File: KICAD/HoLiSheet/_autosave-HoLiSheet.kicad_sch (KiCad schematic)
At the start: 8 parts, among them J1 Conn_01x06, J3 Conn_01x06

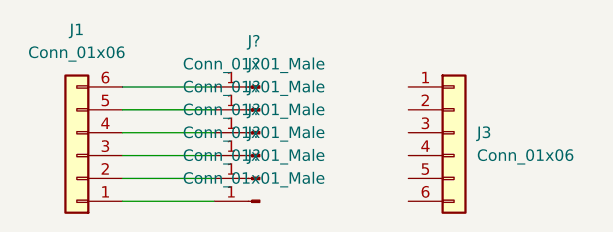
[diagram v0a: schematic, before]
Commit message: Adding new standalone CAD and new iamges
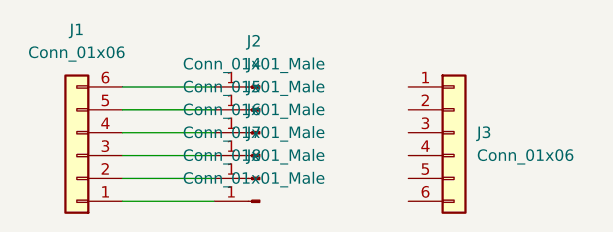
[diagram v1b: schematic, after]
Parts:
- removed J? (x5): Conn_01x01_Male, symbol Connector:Conn_01x01_Male
- added J4, J5, J6, J7, J8: Conn_01x01_Male, footprints:PinHeader_1x01_P1.00mm_Horizontal, symbol Connector:Conn_01x01_Male
- J2: renamed from J?; footprint (none) -> footprints:PinHeader_1x01_P1.00mm_Horizontal
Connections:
- net at J1.1 (Pin_1): now also J8.1 (Pin_1)
- net at J1.2 (Pin_2): now also J7.1 (Pin_1)
- net at J1.3 (Pin_3): now also J6.1 (Pin_1)
- net at J1.4 (Pin_4): now also J5.1 (Pin_1)
- net at J1.5 (Pin_5): now also J4.1 (Pin_1)
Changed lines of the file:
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@@
     (pin "6")
   )
-  (symbol (lib_id "Connector:Conn_01x01_Male") (at 118.11 71.12 180) (unit 1)
+  (symbol (lib_id "Connector:Conn_01x01_Male") (at 118.11 76.2 180) (unit 1)
     (in_bom yes) (on_board yes) (fields_autoplaced)
-    (property "Reference" "J?" (id 0) (at 117.475 66.04 0))
-    (property "Value" "Conn_01x01_Male" (id 1) (at 117.475 68.58 0))
-    (property "Footprint" "" (id 2) (at 118.11 71.12 0)
+    (property "Reference" "J8" (id 0) (at 117.475 71.12 0))
+    (property "Value" "Conn_01x01_Male" (id 1) (at 117.475 73.66 0))
+    (property "Footprint" "footprints:PinHeader_1x01_P1.00mm_Horizontal" (id 2) (at 118.11 76.2 0)
       (effects (font (size 1.27 1.27)) hide)
     )
-    (property "Datasheet" "~" (id 3) (at 118.11 71.12 0)
+    (property "Datasheet" "~" (id 3) (at 118.11 76.2 0)
+      (effects (font (size 1.27 1.27)) hide)
+    )
+    (pin "1")
+  )
+  (symbol (lib_id "Connector:Conn_01x01_Male") (at 118.11 66.04 180) (unit 1)
+    (in_bom yes) (on_board yes) (fields_autoplaced)
+    (property "Reference" "J4" (id 0) (at 117.475 60.96 0))
+    (property "Value" "Conn_01x01_Male" (id 1) (at 117.475 63.5 0))
+    (property "Footprint" "footprints:PinHeader_1x01_P1.00mm_Horizontal" (id 2) (at 118.11 66.04 0)
+      (effects (font (size 1.27 1.27)) hide)
+    )
+    (property "Datasheet" "~" (id 3) (at 118.11 66.04 0)
       (effects (font (size 1.27 1.27)) hide)
     )
@@
   (symbol (lib_id "Connector:Conn_01x01_Male") (at 118.11 68.58 180) (unit 1)
     (in_bom yes) (on_board yes) (fields_autoplaced)
-    (property "Reference" "J?" (id 0) (at 117.475 63.5 0))
+    (property "Reference" "J5" (id 0) (at 117.475 63.5 0))
     (property "Value" "Conn_01x01_Male" (id 1) (at 117.475 66.04 0))
-    (property "Footprint" "" (id 2) (at 118.11 68.58 0)
+    (property "Footprint" "footprints:PinHeader_1x01_P1.00mm_Horizontal" (id 2) (at 118.11 68.58 0)
       (effects (font (size 1.27 1.27)) hide)
     )
     (property "Datasheet" "~" (id 3) (at 118.11 68.58 0)
+      (effects (font (size 1.27 1.27)) hide)
+    )
+    (pin "1")
+  )
+  (symbol (lib_id "Connector:Conn_01x01_Male") (at 118.11 71.12 180) (unit 1)
+    (in_bom yes) (on_board yes) (fields_autoplaced)
+    (property "Reference" "J6" (id 0) (at 117.475 66.04 0))
+    (property "Value" "Conn_01x01_Male" (id 1) (at 117.475 68.58 0))
+    (property "Footprint" "footprints:PinHeader_1x01_P1.00mm_Horizontal" (id 2) (at 118.11 71.12 0)
+      (effects (font (size 1.27 1.27)) hide)
+    )
+    (property "Datasheet" "~" (id 3) (at 118.11 71.12 0)
       (effects (font (size 1.27 1.27)) hide)
     )
@@
     (pin "6")
   )
-  (symbol (lib_id "Connector:Conn_01x01_Male") (at 118.11 66.04 180) (unit 1)
-    (in_bom yes) (on_board yes) (fields_autoplaced)
-    (property "Reference" "J?" (id 0) (at 117.475 60.96 0))
-    (property "Value" "Conn_01x01_Male" (id 1) (at 117.475 63.5 0))
-    (property "Footprint" "" (id 2) (at 118.11 66.04 0)
-      (effects (font (size 1.27 1.27)) hide)
-    )
-    (property "Datasheet" "~" (id 3) (at 118.11 66.04 0)
-      (effects (font (size 1.27 1.27)) hide)
-    )
-    (pin "1")
-  )
   (symbol (lib_id "Connector:Conn_01x01_Male") (at 118.11 73.66 180) (unit 1)
     (in_bom yes) (on_board yes) (fields_autoplaced)
-    (property "Reference" "J?" (id 0) (at 117.475 68.58 0))
+    (property "Reference" "J7" (id 0) (at 117.475 68.58 0))
     (property "Value" "Conn_01x01_Male" (id 1) (at 117.475 71.12 0))
-    (property "Footprint" "" (id 2) (at 118.11 73.66 0)
+    (property "Footprint" "footprints:PinHeader_1x01_P1.00mm_Horizontal" (id 2) (at 118.11 73.66 0)
       (effects (font (size 1.27 1.27)) hide)
     )
@@
     (pin "1")
   )
-  (symbol (lib_id "Connector:Conn_01x01_Male") (at 118.11 76.2 180) (unit 1)
-    (in_bom yes) (on_board yes) (fields_autoplaced)
-    (property "Reference" "J?" (id 0) (at 117.475 71.12 0))
-    (property "Value" "Conn_01x01_Male" (id 1) (at 117.475 73.66 0))
-    (property "Footprint" "" (id 2) (at 118.11 76.2 0)
-      (effects (font (size 1.27 1.27)) hide)
-    )
-    (property "Datasheet" "~" (id 3) (at 118.11 76.2 0)
-      (effects (font (size 1.27 1.27)) hide)
-    )
-    (pin "1")
-  )
   (symbol (lib_id "Connector:Conn_01x01_Male") (at 118.11 63.5 180) (unit 1)
     (in_bom yes) (on_board yes) (fields_autoplaced)
-    (property "Reference" "J?" (id 0) (at 117.475 58.42 0))
+    (property "Reference" "J2" (id 0) (at 117.475 58.42 0))
     (property "Value" "Conn_01x01_Male" (id 1) (at 117.475 60.96 0))
-    (property "Footprint" "" (id 2) (at 118.11 63.5 0)
+    (property "Footprint" "footprints:PinHeader_1x01_P1.00mm_Horizontal" (id 2) (at 118.11 63.5 0)
       (effects (font (size 1.27 1.27)) hide)
     )
@@
       (reference "J1") (unit 1) (value "Conn_01x06") (footprint "Connector_PinHeader_2.54mm:PinHeader_1x06_P2.54mm_Vertical")
     )
+    (path "/fe9ccbbc-a9cf-4886-a19b-9a3d08cdb206"
+      (reference "J2") (unit 1) (value "Conn_01x01_Male") (footprint "footprints:PinHeader_1x01_P1.00mm_Horizontal")
+    )
     (path "/b45faf1e-b7a2-4d73-9833-db84a2fde78b"
       (reference "J3") (unit 1) (value "Conn_01x06") (footprint "Connector_PinHeader_1.00mm:PinHeader_1x06_P1.00mm_Vertical_SMD_Pin1Left")
     )
-    (path "/92b90d16-2c0d-4d75-9dc0-ee4497e2003f"
-      (reference "J?") (unit 1) (value "Conn_01x01_Male") (footprint "")
+    (path "/3d07da88-94bf-458a-a135-40a54152bd97"
+      (reference "J4") (unit 1) (value "Conn_01x01_Male") (footprint "footprints:PinHeader_1x01_P1.00mm_Horizontal")
     )
-    (path "/a31886a6-dcc1-4277-be76-640a1dddba05"
-      (reference "J?") (unit 1) (value "Conn_01x01_Male") (footprint "")
+    (path "/42cd5fde-d496-467b-9aa3-63e7f6326518"
+      (reference "J5") (unit 1) (value "Conn_01x01_Male") (footprint "footprints:PinHeader_1x01_P1.00mm_Horizontal")
     )
-    (path "/cb476e3b-6c69-46c4-81c5-8665ba3f393a"
-      (reference "J?") (unit 1) (value "Conn_01x01_Male") (footprint "")
+    (path "/aeda4e14-9a18-428c-affd-e1707bff9b12"
+      (reference "J6") (unit 1) (value "Conn_01x01_Male") (footprint "footprints:PinHeader_1x01_P1.00mm_Horizontal")
     )
-    (path "/d9bd50c5-028a-493a-8ac9-2dcf6441d81b"
-      (reference "J?") (unit 1) (value "Conn_01x01_Male") (footprint "")
+    (path "/ef3cf04e-682b-44e8-9b07-fc8e4d284ba5"
+      (reference "J7") (unit 1) (value "Conn_01x01_Male") (footprint "footprints:PinHeader_1x01_P1.00mm_Horizontal")
     )
-    (path "/e8bfd87d-f44c-4ddb-b082-3ad63d0d8bd4"
-      (reference "J?") (unit 1) (value "Conn_01x01_Male") (footprint "")
-    )
-    (path "/fe9ccbbc-a9cf-4886-a19b-9a3d08cdb206"
-      (reference "J?") (unit 1) (value "Conn_01x01_Male") (footprint "")
+    (path "/178d70b0-9d36-4b6c-a819-2840526db39a"
+      (reference "J8") (unit 1) (value "Conn_01x01_Male") (footprint "footprints:PinHeader_1x01_P1.00mm_Horizontal")
     )
   )
